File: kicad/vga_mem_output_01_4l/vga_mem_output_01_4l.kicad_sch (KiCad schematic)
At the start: 37 parts, among them J1 Conn_01x03_Socket, J2 Conn_01x02_Socket, J3 Conn_01x08_Socket, J4 DE15_Socket_HighDensity_Mount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, J5 Conn_01x18_Socket, J6 Conn_01x18_Socket, U1 74LS08, U10 74HCT574, U2 74LS08, U3 UM61512, U4 UM61512, U5 74LS157, U6 74LS157, U7 74LS157, U8 74LS157, U9 74LS157

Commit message: added cpu side bus transceiver
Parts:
- added C13, C14: 100nF, Capacitor_SMD:C_0805_2012Metric_Pad1.18x1.45mm_HandSolder, symbol Device:C
- added U11: 74HC245, Package_SO:SO-20_12.8x7.5mm_P1.27mm, symbol 74xx:74HC245
- added U12: 74AHC1GU04, Package_TO_SOT_SMD:SOT-23-5_HandSoldering, symbol 74xGxx:74AHC1GU04
- U10: footprint Package_SO:SO-20_5.3x12.6mm_P1.27mm -> Package_SO:SO-20_12.8x7.5mm_P1.27mm
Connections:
- net ~{OE} is gone; now on net ~{A_FRONT}: U3.24 (~{OE}), U4.24 (~{OE})
- net CPU_A12: now also U8.10 (I1c); no longer U8.11 (I0c)
- net CPU_A13: now also U8.13 (I1d); no longer U8.14 (I0d)
- net DG_A12: now also U8.11 (I0c); no longer U8.10 (I1c)
- net DG_A13: now also U8.14 (I0d); no longer U8.13 (I1d)
- net GND: now also C13.2, C14.2, U11.10 (GND), U12.3 (GND)
- net PDB_1: now also U1.1; no longer U1.9
- net PDB_2: now also U1.4; no longer U1.12
- net PDB_3: now also U1.9; no longer U1.1
- net PDB_4: now also U1.12; no longer U1.4
- net PD_0: now also U11.4 (A2); no longer J3.1 (Pin_1)
- net PD_1: now also U11.6 (A4); no longer J3.2 (Pin_2)
- net PD_2: now also U11.8 (A6); no longer J3.3 (Pin_3)
- net PD_3: now also U11.9 (A7); no longer J3.4 (Pin_4)
- net PD_4: now also U11.7 (A5); no longer J3.5 (Pin_5)
- net PD_5: now also U11.5 (A3); no longer J3.6 (Pin_6)
- net PD_6: now also U11.3 (A1); no longer J3.7 (Pin_7)
- net PD_7: now also U11.2 (A0); no longer J3.8 (Pin_8)
- net VCC: now also C13.1, C14.1, U11.20 (VCC), U12.5 (VCC)
- net ~{A_FRONT}: now also U12.2
- net at R5.1: now also U1.11; no longer U1.6
- net at R2.1: now also U1.3; no longer U1.8
- net at R4.1: now also U1.8; no longer U1.3
- net at R3.1: now also U1.6; no longer U1.11
- new net A_FRONT: U11.19 (CE), U12.4
- new net CPU_D0: J3.1 (Pin_1), U11.16 (B2)
- new net CPU_D1: J3.2 (Pin_2), U11.14 (B4)
- new net CPU_D2: J3.3 (Pin_3), U11.12 (B6)
- new net CPU_D3: J3.4 (Pin_4), U11.11 (B7)
- new net CPU_D4: J3.5 (Pin_5), U11.13 (B5)
- new net CPU_D5: J3.6 (Pin_6), U11.15 (B3)
- new net CPU_D6: J3.7 (Pin_7), U11.17 (B1)
- new net CPU_D7: J3.8 (Pin_8), U11.18 (B0)
- new net CPU_R~{W}: U11.1 (A->B)
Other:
- moved on the sheet: C10, C11, C12, C3, C4, C5, C6, C7, C8, C9, J3, J5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

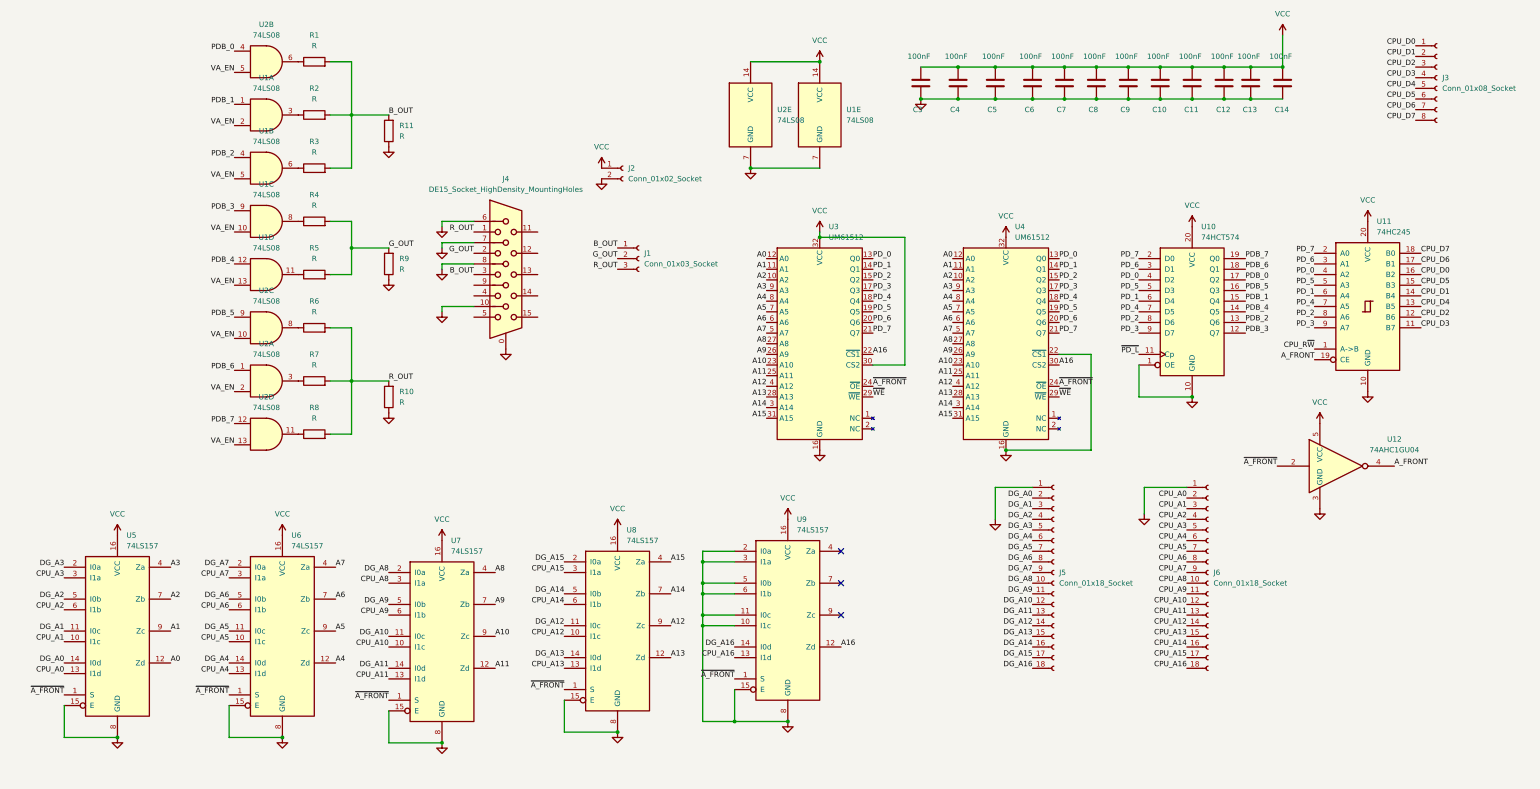
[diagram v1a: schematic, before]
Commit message: 4l vga mem output routing improvements
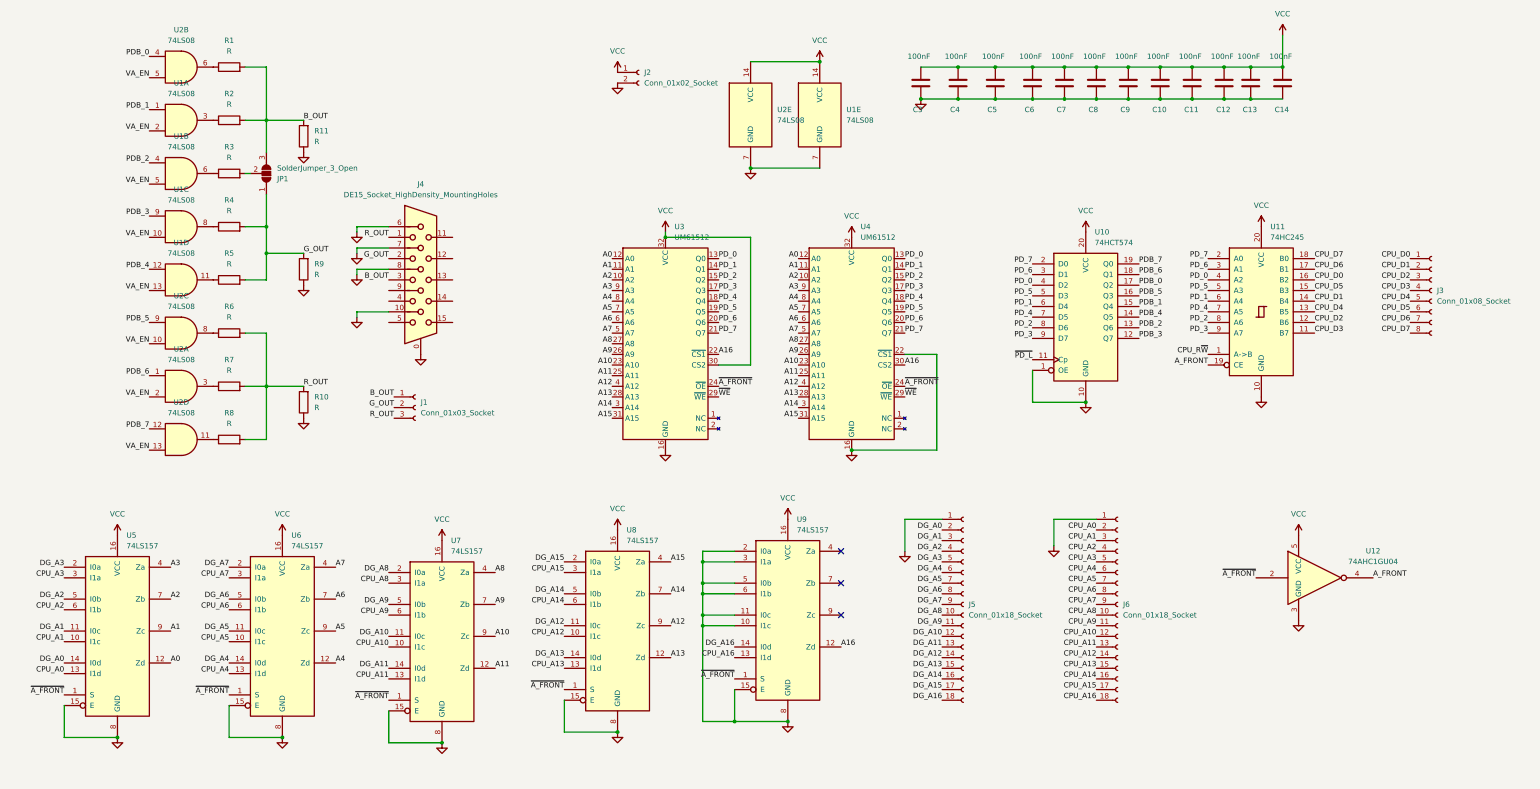
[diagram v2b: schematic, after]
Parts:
- added JP1: SolderJumper_3_Open, Jumper:SolderJumper-3_P1.3mm_Open_RoundedPad1.0x1.5mm, symbol Jumper:SolderJumper_3_Open
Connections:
- net B_OUT: now also JP1.3 (B); no longer R3.2
- net G_OUT: now also JP1.1 (A)
- new net: JP1.2 (C), R3.2
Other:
- moved on the sheet: J1, J2, J3, J4, J5, J6, R1, R10, R11, R2, R3, R4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

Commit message: use hierarchical sheet for vga mem output
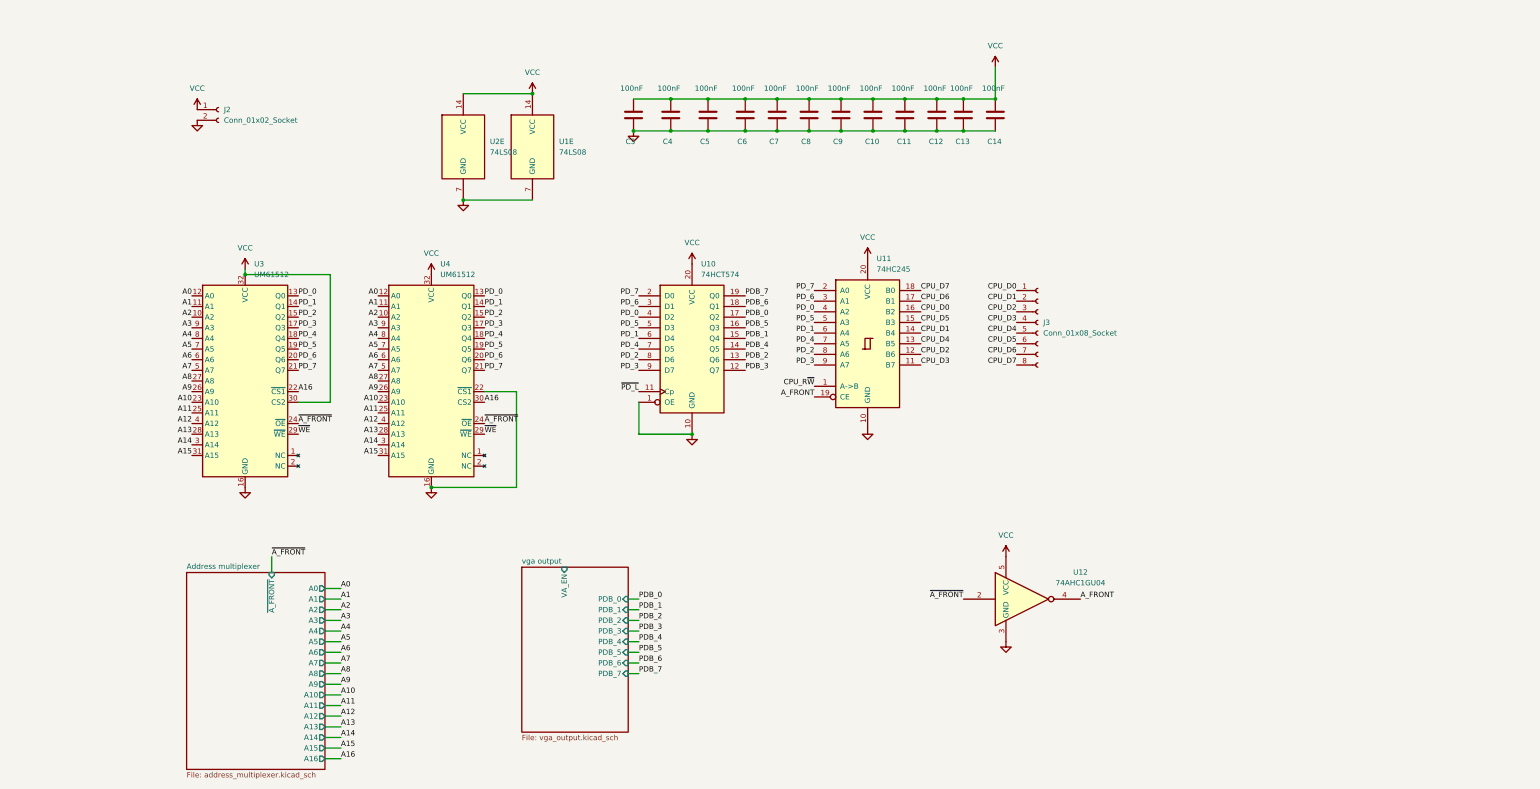
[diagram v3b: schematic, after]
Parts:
- removed J1: Conn_01x03_Socket, Connector_PinSocket_2.54mm:PinSocket_1x03_P2.54mm_Vertical, symbol Connector:Conn_01x03_Socket
- removed J4: DE15_Socket_HighDensity_MountingHoles, Connector_Dsub:DSUB-15-HD_Socket_Horizontal_P2.29x2.54mm_EdgePinOffset8.35mm_Housed_MountingHolesOffset10.89mm, symbol Connector:DE15_Socket_HighDensity_MountingHoles
- removed J5, J6: Conn_01x18_Socket, Connector_PinHeader_2.54mm:PinHeader_1x18_P2.54mm_Vertical, symbol Connector:Conn_01x18_Socket
- removed JP1: SolderJumper_3_Open, Jumper:SolderJumper-3_P1.3mm_Open_RoundedPad1.0x1.5mm, symbol Jumper:SolderJumper_3_Open
- removed R1, R10, R11, R2, R3, R4, R5, R6, R7, R8, R9: R, Resistor_THT:R_Axial_DIN0204_L3.6mm_D1.6mm_P7.62mm_Horizontal, symbol Device:R
- removed unit 4 of U1
- removed unit 3 of U1
- removed unit 1 of U1
- removed unit 2 of U1
- removed unit 1 of U2
- removed unit 2 of U2
- removed unit 3 of U2
- removed unit 4 of U2
- removed U5, U6, U7, U8, U9: 74LS157, Package_SO:SO-16_3.9x9.9mm_P1.27mm, symbol 74xx:74LS157
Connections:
- no-connect marks 3 -> 0
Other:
- added sheet Address multiplexer (address_multiplexer.kicad_sch)
- added sheet vga output (vga_output.kicad_sch)
- moved on the sheet: C10, C11, C12, C13, C14, C3, C4, C5, C6, C7, C8, C9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

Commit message: added clock circuit ('display generator')
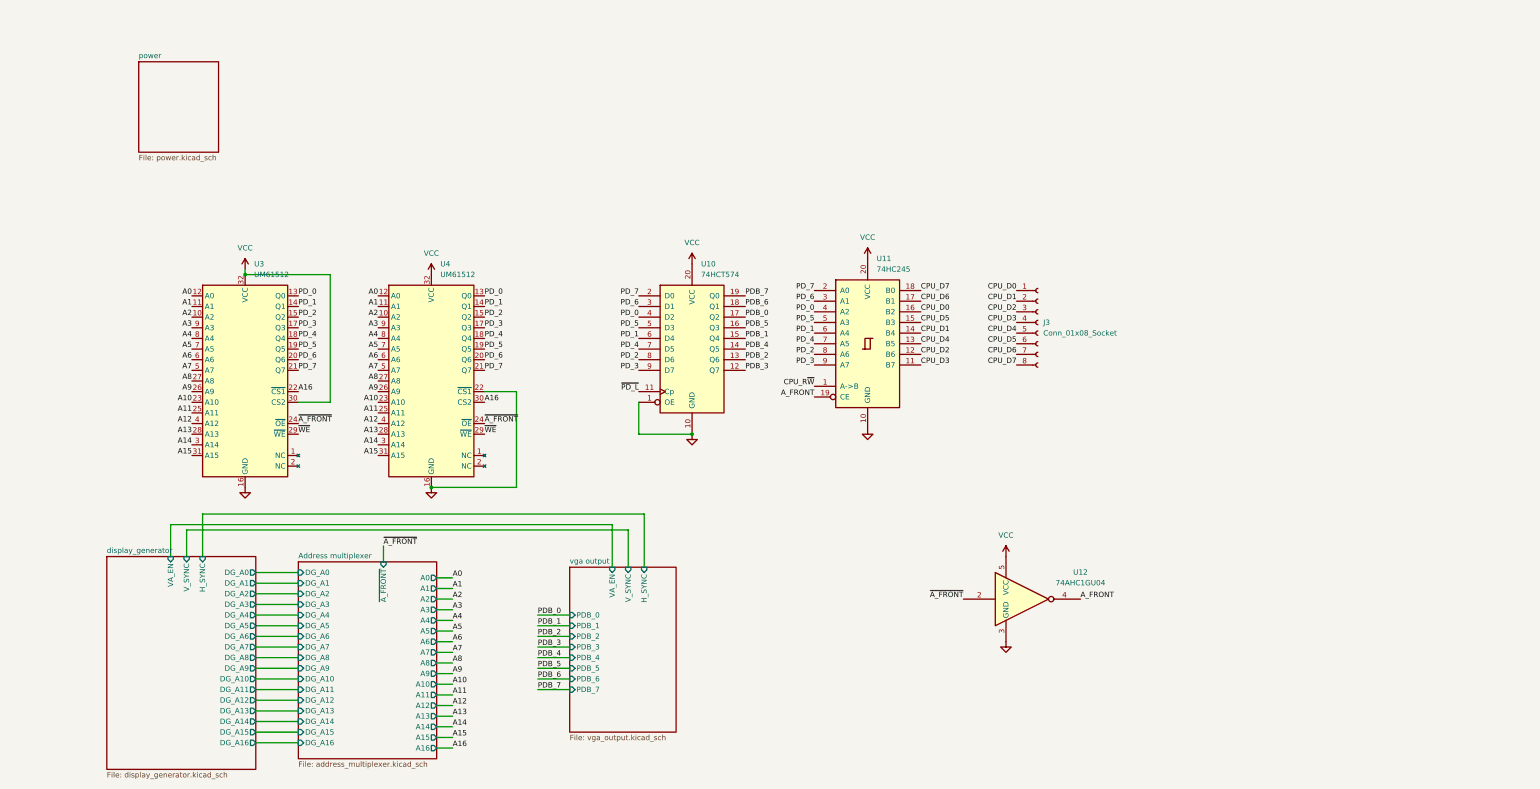
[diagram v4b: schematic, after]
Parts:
- removed C10, C11, C12, C13, C14, C3, C4, C5, C6, C7, C8, C9: 100nF, Capacitor_SMD:C_0805_2012Metric_Pad1.18x1.45mm_HandSolder, symbol Device:C
- removed J2: Conn_01x02_Socket, Connector_PinSocket_2.54mm:PinSocket_1x02_P2.54mm_Vertical, symbol Connector:Conn_01x02_Socket
- removed U1, U2: 74LS08, Package_SO:SO-14_3.9x8.65mm_P1.27mm, symbol 74xx:74LS08
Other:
- added sheet display_generator (display_generator.kicad_sch)
- added sheet power (power.kicad_sch)
- sheet Address multiplexer ports: added DG_A0, DG_A1, DG_A10, DG_A11, DG_A12, DG_A13, DG_A14, DG_A15, DG_A16, DG_A2, DG_A3, DG_A4, DG_A5, DG_A6, DG_A7, DG_A8, DG_A9; removed none
- sheet vga output ports: added H_SYNC, V_SYNC; removed none

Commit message: routing fixes
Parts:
- added J1: Conn_01x03_Socket, Connector_PinSocket_2.54mm:PinSocket_1x03_P2.54mm_Vertical, symbol Connector:Conn_01x03_Socket
- added JP2: SolderJumper_3_Open, Jumper:SolderJumper-3_P1.3mm_Open_RoundedPad1.0x1.5mm, symbol Jumper:SolderJumper_3_Open
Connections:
- net ~{A_FRONT}: now also J1.1 (Pin_1)
- net ~{PD_L}: now also JP2.2 (C)
- net ~{WE}: now also J1.2 (Pin_2)
- new net H0_EXT: J1.3 (Pin_3), JP2.1 (A)
- new net display_generator/DG_PIXEL: JP2.3 (B)
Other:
- sheet display_generator ports: added DG_PIXEL; removed none
- moved on the sheet: J3, U12, U3, U4

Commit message: switch to VCC pour on signal layers, revised signal / ref assignments
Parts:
- J1: footprint Connector_PinSocket_2.54mm:PinSocket_1x03_P2.54mm_Vertical -> Connector_PinSocket_2.54mm:PinSocket_1x04_P2.54mm_Vertical; symbol Connector:Conn_01x03_Socket -> Connector:Conn_01x04_Socket
- J3: footprint Connector_PinSocket_2.54mm:PinSocket_1x08_P2.54mm_Vertical -> Connector_PinSocket_2.54mm:PinSocket_1x09_P2.54mm_Vertical; symbol Connector:Conn_01x08_Socket -> Connector:Conn_01x09_Socket
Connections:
- net CPU_D0: now also J3.2 (Pin_2); no longer J3.1 (Pin_1)
- net CPU_D1: now also J3.3 (Pin_3); no longer J3.2 (Pin_2)
- net CPU_D2: now also J3.4 (Pin_4); no longer J3.3 (Pin_3)
- net CPU_D3: now also J3.5 (Pin_5); no longer J3.4 (Pin_4)
- net CPU_D4: now also J3.6 (Pin_6); no longer J3.5 (Pin_5)
- net CPU_D5: now also J3.7 (Pin_7); no longer J3.6 (Pin_6)
- net CPU_D6: now also J3.8 (Pin_8); no longer J3.7 (Pin_7)
- net CPU_D7: now also J3.9 (Pin_9); no longer J3.8 (Pin_8)
- net GND: now also J1.1 (Pin_1), J3.1 (Pin_1)
- net H0_EXT: now also J1.4 (Pin_4); no longer J1.3 (Pin_3)
- net ~{A_FRONT}: now also J1.2 (Pin_2); no longer J1.1 (Pin_1)
- net ~{WE}: now also J1.3 (Pin_3); no longer J1.2 (Pin_2)
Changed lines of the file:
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@@
+	(wire
+		(pts
+			(xy 233.68 85.09) (xy 233.68 71.12)
+		)
+		(stroke
+			(width 0)
+			(type default)
+		)
+	)
 	(wire
 		(pts
@@
 	(wire
 		(pts
+			(xy 232.41 107.95) (xy 232.41 96.52)
+		)
+		(stroke
+			(width 0)
+			(type default)
+		)
+	)
+	(wire
+		(pts
 			(xy 101.6 165.1) (xy 97.79 165.1)
+		)
+		(stroke
+			(width 0)
+			(type default)
+		)
+	)
+	(wire
+		(pts
+			(xy 232.41 96.52) (xy 243.84 96.52)
+		)
+		(stroke
+			(width 0)
+			(type default)
+		)
+	)
+	(wire
+		(pts
+			(xy 233.68 71.12) (xy 245.11 71.12)
 		)
 		(stroke
@@
 	)
 	(symbol
-		(lib_id "Connector:Conn_01x08_Socket")
+		(lib_id "power:GND")
+		(at 233.68 85.09 0)
+		(unit 1)
+		(exclude_from_sim no)
+		(in_bom yes)
+		(on_board yes)
+		(dnp no)
+		(fields_autoplaced yes)
+		(property "Reference" "#PWR022"
+			(at 233.68 91.44 0)
+			(effects
+				(font
+					(size 1.27 1.27)
+				)
+				(hide yes)
+			)
+		)
+		(property "Value" "GND"
+			(at 233.68 90.17 0)
+			(effects
+				(font
+					(size 1.27 1.27)
+				)
+			)
+		)
+		(property "Footprint" ""
+			(at 233.68 85.09 0)
+			(effects
+				(font
+					(size 1.27 1.27)
+				)
+				(hide yes)
+			)
+		)
+		(property "Datasheet" ""
+			(at 233.68 85.09 0)
+			(effects
+				(font
+					(size 1.27 1.27)
+				)
+				(hide yes)
+			)
+		)
+		(property "Description" "Power symbol creates a global label with name \"GND\" , ground"
+			(at 233.68 85.09 0)
+			(effects
+				(font
+					(size 1.27 1.27)
+				)
+				(hide yes)
+			)
+		)
+		(pin "1"
+		)
+		(instances
+			(project ""
+				(path "/cb13e431-64f0-4016-a936-ee98aca3391f"
+					(reference "#PWR022")
+					(unit 1)
+				)
+			)
+		)
+	)
+	(symbol
+		(lib_id "Connector:Conn_01x09_Socket")
 		(at 250.19 81.28 0)
 		(unit 1)
@@
 		(fields_autoplaced yes)
 		(property "Reference" "J3"
-			(at 251.46 81.2799 0)
+			(at 251.46 80.0099 0)
 			(effects
 				(font
@@
 		)
 		(property "Value" "Conn_01x08_Socket"
-			(at 251.46 83.8199 0)
+			(at 251.46 82.5499 0)
 			(effects
 				(font
@@
 			)
 		)
-		(property "Footprint" "Connector_PinSocket_2.54mm:PinSocket_1x08_P2.54mm_Vertical"
+		(property "Footprint" "Connector_PinSocket_2.54mm:PinSocket_1x09_P2.54mm_Vertical"
 			(at 250.19 81.28 0)
 			(effects
@@
 			)
 		)
-		(property "Description" "Generic connector, single row, 01x08, script generated"
+		(property "Description" "Generic connector, single row, 01x09, script generated"
 			(at 250.19 81.28 0)
 			(effects
@@
 		)
 		(pin "6"
+		)
+		(pin "9"
 		)
 		(instances
@@
 	)
 	(symbol
-		(lib_id "Connector:Conn_01x03_Socket")
-		(at 248.92 101.6 0)
+		(lib_id "Connector:Conn_01x04_Socket")
+		(at 248.92 99.06 0)
 		(unit 1)
 		(exclude_from_sim no)
@@
 		(fields_autoplaced yes)
 		(property "Reference" "J1"
-			(at 250.19 100.3299 0)
+			(at 250.19 99.0599 0)
 			(effects
 				(font
@@
 		)
 		(property "Value" "Conn_01x03_Socket"
-			(at 250.19 102.8699 0)
+			(at 250.19 101.5999 0)
 			(effects
 				(font
@@
 			)
 		)
-		(property "Footprint" "Connector_PinSocket_2.54mm:PinSocket_1x03_P2.54mm_Vertical"
-			(at 248.92 101.6 0)
+		(property "Footprint" "Connector_PinSocket_2.54mm:PinSocket_1x04_P2.54mm_Vertical"
+			(at 248.92 99.06 0)
 			(effects
 				(font
@@
 		)
 		(property "Datasheet" "~"
-			(at 248.92 101.6 0)
-			(effects
-				(font
-					(size 1.27 1.27)
-				)
-				(hide yes)
-			)
-		)
-		(property "Description" "Generic connector, single row, 01x03, script generated"
-			(at 248.92 101.6 0)
+			(at 248.92 99.06 0)
+			(effects
+				(font
+					(size 1.27 1.27)
+				)
+				(hide yes)
+			)
+		)
+		(property "Description" "Generic connector, single row, 01x04, script generated"
+			(at 248.92 99.06 0)
 			(effects
 				(font
@@
 		)
 		(pin "1"
+		)
+		(pin "4"
 		)
 		(instances
@@
 					(unit 1)
 				)
+			)
+		)
+	)
+	(symbol
+		(lib_id "power:GND")
+		(at 232.41 107.95 0)
+		(unit 1)
+		(exclude_from_sim no)
+		(in_bom yes)
+		(on_board yes)
+		(dnp no)
+		(fields_autoplaced yes)
+		(property "Reference" "#PWR054"
+			(at 232.41 114.3 0)
+			(effects
+				(font
+					(size 1.27 1.27)
+				)
+				(hide yes)
+			)
+		)
+		(property "Value" "GND"
+			(at 232.41 113.03 0)
+			(effects
+				(font
+					(size 1.27 1.27)
+				)
+			)
+		)
+		(property "Footprint" ""
+			(at 232.41 107.95 0)
+			(effects
+				(font
+					(size 1.27 1.27)
+				)
+				(hide yes)
+			)
+		)
+		(property "Datasheet" ""
+			(at 232.41 107.95 0)
+			(effects
+				(font
+					(size 1.27 1.27)
+				)
+				(hide yes)
+			)
+		)
+		(property "Description" "Power symbol creates a global label with name \"GND\" , ground"
+			(at 232.41 107.95 0)
+			(effects
+				(font
+					(size 1.27 1.27)
+				)
+				(hide yes)
+			)
+		)
+		(pin "1"
+		)
+		(instances
+			(project "vga_mem_output_01_4l"
+				(path "/cb13e431-64f0-4016-a936-ee98aca3391f"
+					(reference "#PWR054")
+					(unit 1)
+				)
